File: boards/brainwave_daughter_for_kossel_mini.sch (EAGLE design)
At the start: 18 parts, among them U6 7805

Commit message: finished first draft of extruder and daughter boards
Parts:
- removed C22, C23: 1uF, rcl:C-USC0603
- removed C28, C29: 47uF, rcl:CPOL-US153CLV-0605
- removed E: (no value), con-lstb:MA04-2
- removed U6: 7805, shinythings:78
- added BED_LED_HEDR: (no value), con-lstb:MA03-1
- added D0_LMT_HEDR, D1_LMT_HEDR, D2_LMT_HEDR: (no value), jumper:JP1E
- added EXTRUDER_HEDR: (no value), con-lstb:MA05-2
- added EXTRUDER_MOTOR_HEDR: (no value), con-lstb:MA04-1
- added EXTRUDER_SOCKET, LED_HEDR: (no value), con-lstb:MA04-2
- added PLUG: (no value), con-wago-500:W237-102
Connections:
- new net N$1: D0_LMT_HEDR.1, X_MIN.1
- new net N$10: EXTRUDER_MOTOR_HEDR.3, EXTRUDER_SOCKET.5
- new net N$11: EXTRUDER_MOTOR_HEDR.4, EXTRUDER_SOCKET.7
- new net N$2: D1_LMT_HEDR.1, Y_MIN.1
- new net N$3: D2_LMT_HEDR.1, Z_MIN.1
- new net N$4: D2_LMT_HEDR.2, Z_MIN.2
- new net N$5: D1_LMT_HEDR.2, Y_MIN.2
- new net N$6: D0_LMT_HEDR.2, X_MIN.2
- new net N$7: EXTRUDER_HEDR.1, FAN.1
- new net N$8: EXTRUDER_MOTOR_HEDR.1, EXTRUDER_SOCKET.1
- new net N$9: EXTRUDER_MOTOR_HEDR.2, EXTRUDER_SOCKET.3
- net +12V: now also EXTRUDER_HEDR.10, EXTRUDER_HEDR.8, PLUG-2.KL; no longer C22.1, C29.+, E.8, U6.IN
- net E_POWER: now also EXTRUDER_HEDR.2, EXTRUDER_HEDR.4, EXTRUDER_SOCKET.6; no longer E.6
- net E_TEMP: now also EXTRUDER_HEDR.9, EXTRUDER_SOCKET.2; no longer E.2
- net GND: now also BED_LED_HEDR.3, EXTRUDER_HEDR.5, EXTRUDER_HEDR.6, EXTRUDER_SOCKET.4, LED_HEDR.2, LED_HEDR.4, LED_HEDR.6, LED_HEDR.8, PLUG-1.KL; no longer C22.2, C23.2, C28.-, C29.-, E.4, U6.GND
- net MISO: now also EXTRUDER_HEDR.7
- net MOSI: now also BED_LED_HEDR.1
- net VCC: now also BED_LED_HEDR.2, EXTRUDER_HEDR.3, LED_HEDR.1, LED_HEDR.3, LED_HEDR.5, LED_HEDR.7; no longer C23.1, C28.+, U6.OUT
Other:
- note removed: "Open Source Hardware"
- moved on the sheet: FAN, H1, H2, H3, H4, ICSP, X1-1, X1-2, X2-1, X2-2, X3-1, X3-2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

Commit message: replaced 2x5 header with 2x4 header
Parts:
- EXTRUDER_HEDR: device con-lstb:MA05-2 -> con-lstb:MA04-2
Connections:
- removed net MOSI: BED_LED_HEDR.1, ICSP.4
- net +12V: now also EXTRUDER_HEDR.1; no longer EXTRUDER_HEDR.10, EXTRUDER_HEDR.8
- net E_POWER: now also EXTRUDER_HEDR.7; no longer EXTRUDER_HEDR.2, EXTRUDER_HEDR.4
- net E_TEMP: now also EXTRUDER_HEDR.3; no longer EXTRUDER_HEDR.9
- net GND: now also EXTRUDER_HEDR.4; no longer EXTRUDER_HEDR.5, EXTRUDER_HEDR.6
- net MISO: now also EXTRUDER_HEDR.2; no longer EXTRUDER_HEDR.7
- net N$7: now also EXTRUDER_HEDR.8; no longer EXTRUDER_HEDR.1
- net SCK: now also BED_LED_HEDR.1
- net VCC: now also EXTRUDER_HEDR.6; no longer EXTRUDER_HEDR.3
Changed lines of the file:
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@@
 <part name="D1_LMT_HEDR" library="jumper" deviceset="JP1E" device=""/>
 <part name="D2_LMT_HEDR" library="jumper" deviceset="JP1E" device=""/>
-<part name="EXTRUDER_HEDR" library="con-lstb" deviceset="MA05-2" device=""/>
 <part name="GND2" library="supply1" deviceset="GND" device=""/>
 <part name="P+2" library="supply1" deviceset="+12V" device=""/>
@@
 <part name="P+5" library="supply1" deviceset="VCC" device=""/>
 <part name="P+6" library="supply1" deviceset="VCC" device=""/>
+<part name="EXTRUDER_HEDR" library="con-lstb" deviceset="MA04-2" device=""/>
 </parts>
 <sheets>
@@
 <instance part="D1_LMT_HEDR" gate="A" x="551.18" y="-5.08"/>
 <instance part="D2_LMT_HEDR" gate="A" x="561.34" y="-5.08"/>
-<instance part="EXTRUDER_HEDR" gate="G$1" x="665.48" y="33.02" rot="R180"/>
 <instance part="GND2" gate="1" x="650.24" y="7.62"/>
 <instance part="P+2" gate="1" x="695.96" y="38.1"/>
@@
 <instance part="P+5" gate="VCC" x="563.88" y="53.34"/>
 <instance part="P+6" gate="VCC" x="637.54" y="45.72"/>
+<instance part="EXTRUDER_HEDR" gate="G$1" x="665.48" y="35.56"/>
 </instances>
 <busses>
@@
 </segment>
 <segment>
-<pinref part="EXTRUDER_HEDR" gate="G$1" pin="3"/>
 <wire x1="657.86" y1="35.56" x2="637.54" y2="35.56" width="0.1524" layer="91"/>
 <pinref part="P+6" gate="VCC" pin="VCC"/>
 <wire x1="637.54" y1="35.56" x2="637.54" y2="43.18" width="0.1524" layer="91"/>
+<pinref part="EXTRUDER_HEDR" gate="G$1" pin="6"/>
 </segment>
 </net>
@@
 </segment>
 <segment>
-<pinref part="EXTRUDER_HEDR" gate="G$1" pin="5"/>
 <pinref part="GND2" gate="1" pin="GND"/>
 <wire x1="657.86" y1="33.02" x2="650.24" y2="33.02" width="0.1524" layer="91"/>
-<wire x1="650.24" y1="33.02" x2="650.24" y2="17.78" width="0.1524" layer="91"/>
-<pinref part="EXTRUDER_HEDR" gate="G$1" pin="6"/>
-<wire x1="650.24" y1="17.78" x2="650.24" y2="10.16" width="0.1524" layer="91"/>
-<wire x1="673.1" y1="33.02" x2="675.64" y2="33.02" width="0.1524" layer="91"/>
-<wire x1="675.64" y1="33.02" x2="675.64" y2="17.78" width="0.1524" layer="91"/>
-<wire x1="675.64" y1="17.78" x2="650.24" y2="17.78" width="0.1524" layer="91"/>
-<junction x="650.24" y="17.78"/>
+<wire x1="650.24" y1="33.02" x2="650.24" y2="10.16" width="0.1524" layer="91"/>
+<pinref part="EXTRUDER_HEDR" gate="G$1" pin="4"/>
 </segment>
 <segment>
@@
 </segment>
 <segment>
-<pinref part="EXTRUDER_HEDR" gate="G$1" pin="10"/>
 <pinref part="P+2" gate="1" pin="+12V"/>
-<wire x1="673.1" y1="27.94" x2="695.96" y2="27.94" width="0.1524" layer="91"/>
-<wire x1="695.96" y1="27.94" x2="695.96" y2="30.48" width="0.1524" layer="91"/>
-<junction x="695.96" y="30.48"/>
 <wire x1="695.96" y1="30.48" x2="695.96" y2="35.56" width="0.1524" layer="91"/>
-<pinref part="EXTRUDER_HEDR" gate="G$1" pin="8"/>
 <wire x1="673.1" y1="30.48" x2="695.96" y2="30.48" width="0.1524" layer="91"/>
+<pinref part="EXTRUDER_HEDR" gate="G$1" pin="1"/>
 </segment>
 <segment>
@@
 </segment>
 </net>
-<net name="MOSI" class="0">
-<segment>
-<pinref part="ICSP" gate="1" pin="4"/>
-<wire x1="612.14" y1="27.94" x2="622.3" y2="27.94" width="0.1524" layer="91"/>
+<net name="SCK" class="0">
+<segment>
 <label x="619.76" y="27.94" size="1.778" layer="95" rot="MR0"/>
 <pinref part="BED_LED_HEDR" gate="G$1" pin="1"/>
-<wire x1="594.36" y1="-5.08" x2="622.3" y2="-5.08" width="0.1524" layer="91"/>
-<wire x1="622.3" y1="-5.08" x2="622.3" y2="27.94" width="0.1524" layer="91"/>
+<wire x1="594.36" y1="-5.08" x2="609.6" y2="-5.08" width="0.1524" layer="91"/>
+<wire x1="609.6" y1="-5.08" x2="609.6" y2="15.24" width="0.1524" layer="91"/>
+<wire x1="609.6" y1="15.24" x2="586.74" y2="15.24" width="0.1524" layer="91"/>
+<wire x1="586.74" y1="15.24" x2="586.74" y2="27.94" width="0.1524" layer="91"/>
+<pinref part="ICSP" gate="1" pin="3"/>
+<wire x1="596.9" y1="27.94" x2="586.74" y2="27.94" width="0.1524" layer="91"/>
+<label x="589.28" y="27.94" size="1.778" layer="95"/>
 </segment>
 </net>
@@
 <wire x1="596.9" y1="25.4" x2="589.28" y2="25.4" width="0.1524" layer="91"/>
 <label x="589.28" y="25.4" size="1.778" layer="95"/>
-</segment>
-</net>
-<net name="SCK" class="0">
-<segment>
-<pinref part="ICSP" gate="1" pin="3"/>
-<wire x1="596.9" y1="27.94" x2="589.28" y2="27.94" width="0.1524" layer="91"/>
-<label x="589.28" y="27.94" size="1.778" layer="95"/>
 </segment>
 </net>
@@
 <wire x1="584.2" y1="43.18" x2="629.92" y2="43.18" width="0.1524" layer="91"/>
 <wire x1="629.92" y1="43.18" x2="629.92" y2="30.48" width="0.1524" layer="91"/>
-<pinref part="EXTRUDER_HEDR" gate="G$1" pin="7"/>
 <wire x1="629.92" y1="30.48" x2="657.86" y2="30.48" width="0.1524" layer="91"/>
+<pinref part="EXTRUDER_HEDR" gate="G$1" pin="2"/>
 </segment>
 </net>
@@
 <segment>
 <pinref part="EXTRUDER_SOCKET" gate="G$1" pin="2"/>
-<wire x1="673.1" y1="-15.24" x2="680.72" y2="-15.24" width="0.1524" layer="91"/>
+<wire x1="673.1" y1="-15.24" x2="678.18" y2="-15.24" width="0.1524" layer="91"/>
 <label x="675.64" y="-5.08" size="1.778" layer="95" rot="MR0"/>
-<wire x1="655.32" y1="27.94" x2="655.32" y2="-5.08" width="0.1524" layer="91"/>
-<wire x1="655.32" y1="-5.08" x2="680.72" y2="-5.08" width="0.1524" layer="91"/>
-<wire x1="680.72" y1="-15.24" x2="680.72" y2="-5.08" width="0.1524" layer="91"/>
-<pinref part="EXTRUDER_HEDR" gate="G$1" pin="9"/>
-<wire x1="655.32" y1="27.94" x2="657.86" y2="27.94" width="0.1524" layer="91"/>
+<wire x1="678.18" y1="33.02" x2="678.18" y2="-15.24" width="0.1524" layer="91"/>
+<wire x1="678.18" y1="33.02" x2="673.1" y2="33.02" width="0.1524" layer="91"/>
+<pinref part="EXTRUDER_HEDR" gate="G$1" pin="3"/>
 </segment>
 </net>
@@
 <wire x1="673.1" y1="-20.32" x2="683.26" y2="-20.32" width="0.1524" layer="91"/>
 <label x="683.26" y="10.16" size="1.778" layer="95" rot="MR270"/>
-<wire x1="683.26" y1="-20.32" x2="683.26" y2="35.56" width="0.1524" layer="91"/>
-<pinref part="EXTRUDER_HEDR" gate="G$1" pin="4"/>
-<wire x1="683.26" y1="35.56" x2="673.1" y2="35.56" width="0.1524" layer="91"/>
-<wire x1="683.26" y1="35.56" x2="683.26" y2="38.1" width="0.1524" layer="91"/>
-<pinref part="EXTRUDER_HEDR" gate="G$1" pin="2"/>
+<wire x1="683.26" y1="-20.32" x2="683.26" y2="38.1" width="0.1524" layer="91"/>
 <wire x1="683.26" y1="38.1" x2="673.1" y2="38.1" width="0.1524" layer="91"/>
-<junction x="683.26" y="35.56"/>
+<pinref part="EXTRUDER_HEDR" gate="G$1" pin="7"/>
 </segment>
 </net>
@@
 <net name="N$7" class="0">
 <segment>
-<pinref part="EXTRUDER_HEDR" gate="G$1" pin="1"/>
 <pinref part="FAN" gate="A" pin="1"/>
 <wire x1="657.86" y1="38.1" x2="645.16" y2="38.1" width="0.1524" layer="91"/>
 <wire x1="645.16" y1="38.1" x2="645.16" y2="43.18" width="0.1524" layer="91"/>
-</segment>
-</net>
+<pinref part="EXTRUDER_HEDR" gate="G$1" pin="8"/>
+</segment>
+</net>

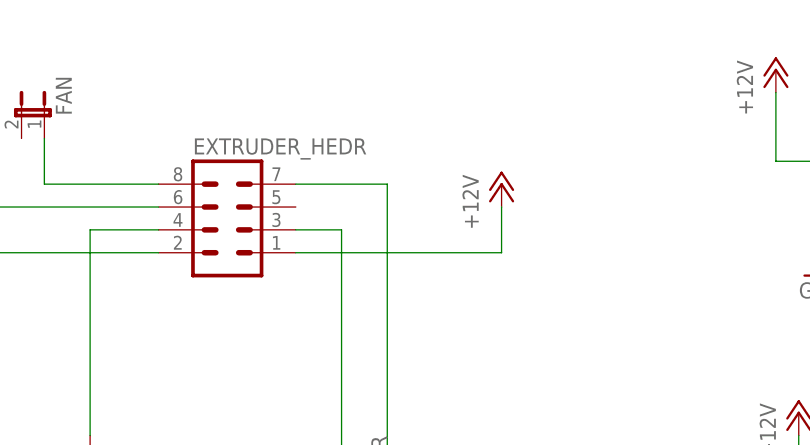
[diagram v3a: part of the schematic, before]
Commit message: put fan on separate 12V supply line
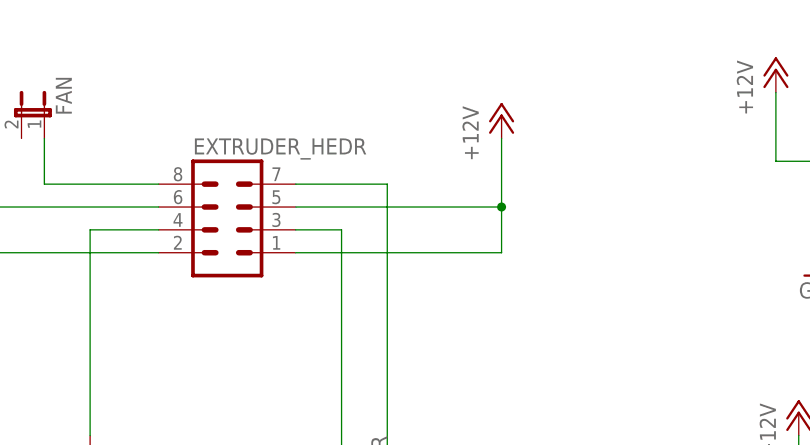
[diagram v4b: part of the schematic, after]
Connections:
- net +12V: now also EXTRUDER_HEDR.5
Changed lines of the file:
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@@
 <instance part="D2_LMT_HEDR" gate="A" x="561.34" y="-5.08"/>
 <instance part="GND2" gate="1" x="650.24" y="7.62"/>
-<instance part="P+2" gate="1" x="695.96" y="38.1"/>
+<instance part="P+2" gate="1" x="695.96" y="45.72"/>
 <instance part="GND3" gate="1" x="601.98" y="-17.78"/>
 <instance part="P+3" gate="VCC" x="596.9" y="12.7"/>
@@
 <pinref part="P+2" gate="1" pin="+12V"/>
 <wire x1="695.96" y1="30.48" x2="695.96" y2="35.56" width="0.1524" layer="91"/>
+<wire x1="695.96" y1="35.56" x2="695.96" y2="43.18" width="0.1524" layer="91"/>
 <wire x1="673.1" y1="30.48" x2="695.96" y2="30.48" width="0.1524" layer="91"/>
 <pinref part="EXTRUDER_HEDR" gate="G$1" pin="1"/>
+<pinref part="EXTRUDER_HEDR" gate="G$1" pin="5"/>
+<wire x1="673.1" y1="35.56" x2="695.96" y2="35.56" width="0.1524" layer="91"/>
+<junction x="695.96" y="35.56"/>
 </segment>
 <segment>
